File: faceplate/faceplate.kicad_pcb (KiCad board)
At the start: 2 copper layers, 30 x 128.5 mm, 8 parts, among them J2 Input Ch1, J3 Input Ch2, J4 Output Ch1, J5 Output Ch2

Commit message: Added basic UI
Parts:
- moved AMP_CH1 47.9 mm to (200.3, 61.0)
- moved AMP_CH2 47.9 mm to (200.3, 101.6)
- moved J2 47.9 mm to (195.2, 134.6)
- moved J3 47.9 mm to (205.4, 134.6)
- moved J4 47.9 mm to (195.2, 147.3)
- moved J5 47.9 mm to (205.4, 147.3)
- moved OFFSET_CH1 47.9 mm to (200.3, 81.3)
- moved OFFSET_CH2 47.9 mm to (200.3, 121.9)

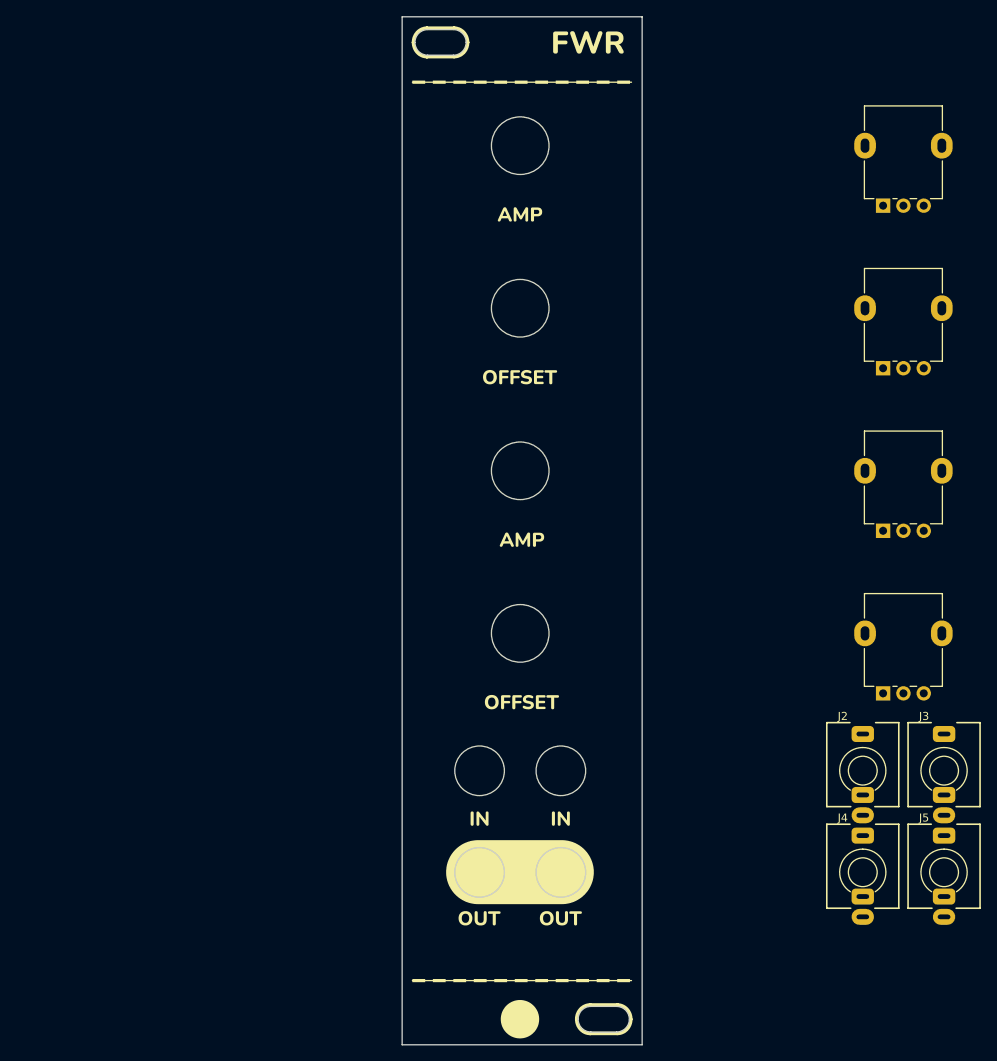
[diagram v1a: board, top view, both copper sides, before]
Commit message: Sync sizes of both modules
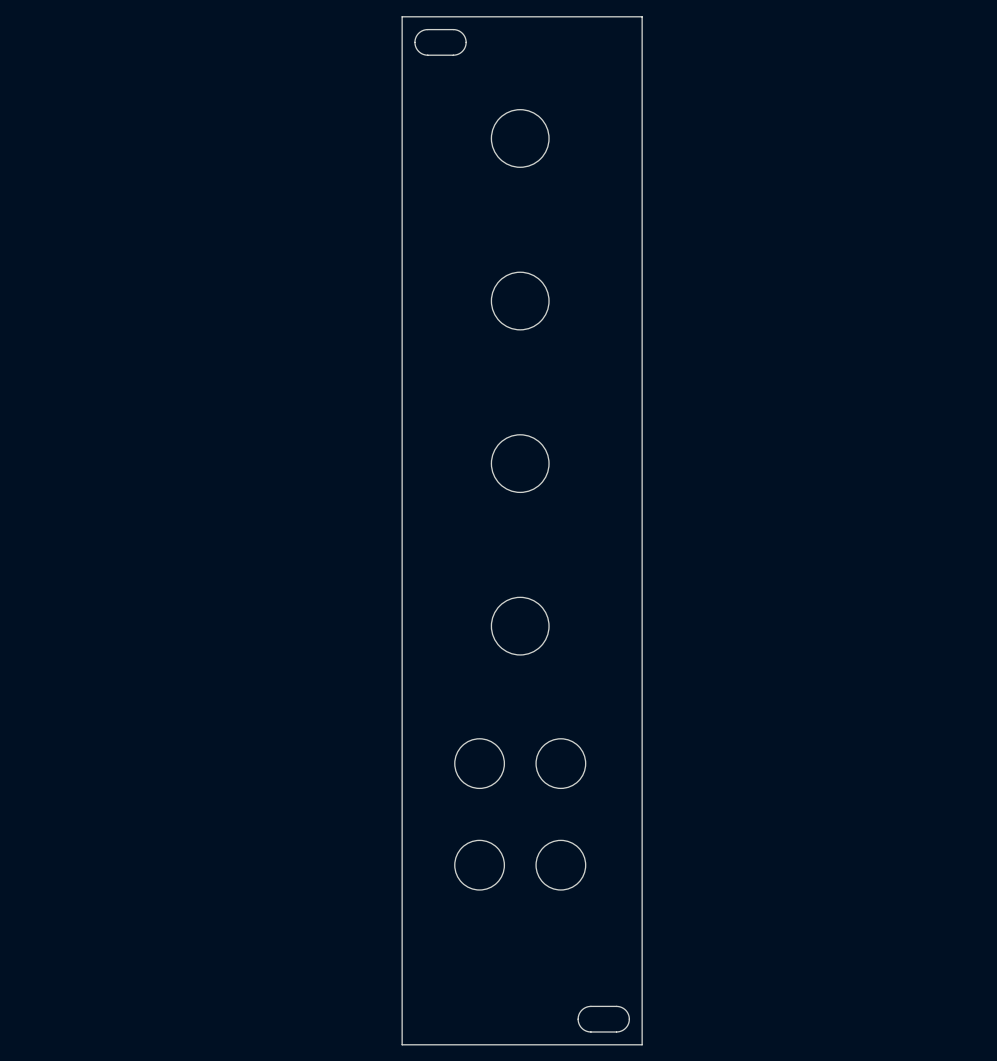
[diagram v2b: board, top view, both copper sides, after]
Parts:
- removed AMP_CH1, AMP_CH2, OFFSET_CH1, OFFSET_CH2: 10k, Eurorack:Pot_Alpha_9mm
- removed J2: Input Ch1, Eurorack:Jack_3.5mm_WQP518MA
- removed J3: Input Ch2, Eurorack:Jack_3.5mm_WQP518MA
- removed J4: Output Ch1, Eurorack:Jack_3.5mm_WQP518MA
- removed J5: Output Ch2, Eurorack:Jack_3.5mm_WQP518MA
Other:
- outline, holes or cut-outs redrawn
